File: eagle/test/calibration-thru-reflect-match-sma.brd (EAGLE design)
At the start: 10 x 44 mm, 6 parts, among them J1 142-0701-851, J2 142-0701-851, J3 142-0701-851, J4 142-0701-851

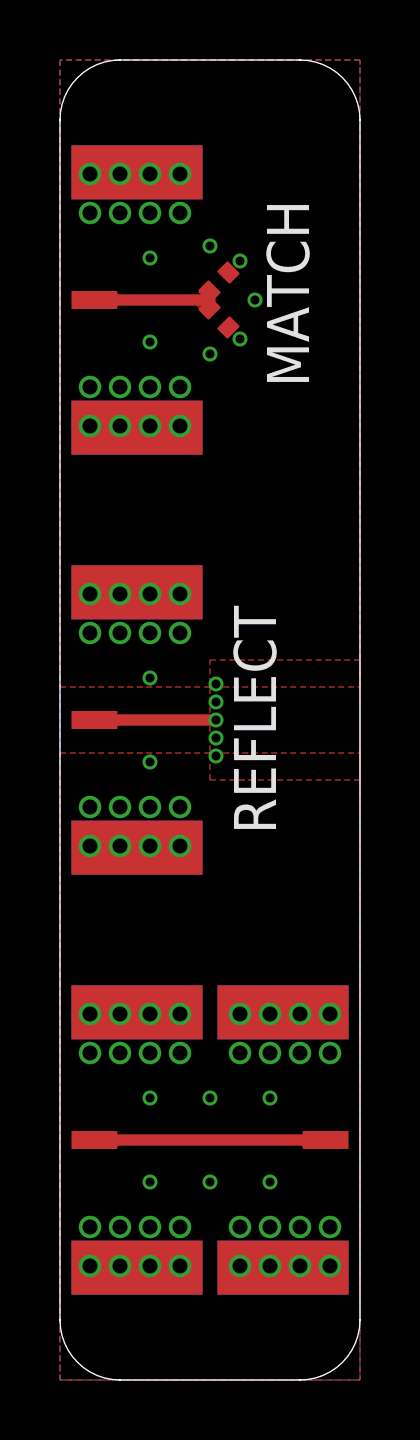
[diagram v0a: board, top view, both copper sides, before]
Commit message: Update TRM kit, add more stop mask around match
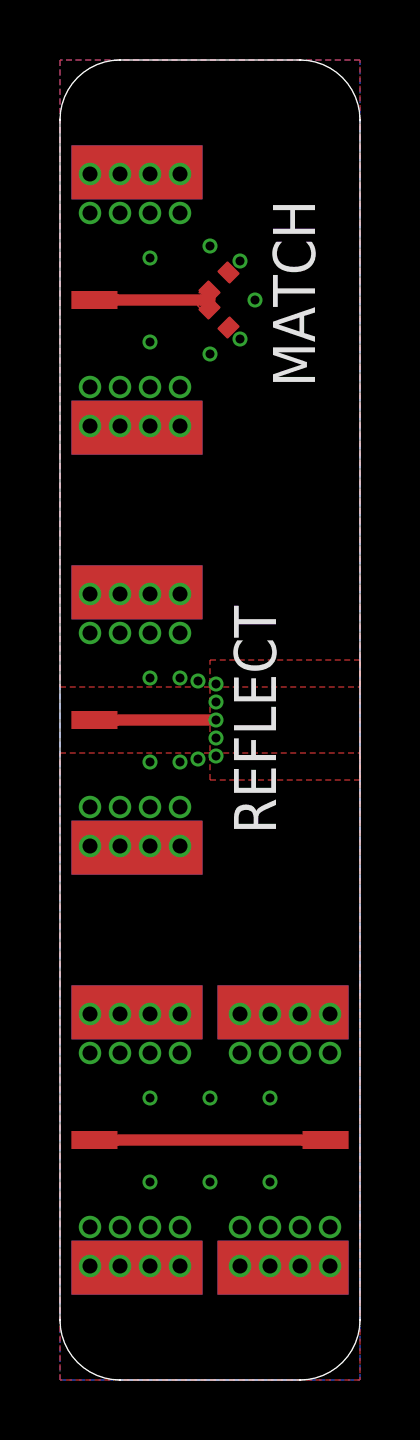
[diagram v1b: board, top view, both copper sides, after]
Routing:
- net GND: vias 84 -> 88
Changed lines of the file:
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@@
 <wire x1="2" y1="0" x2="8" y2="0" width="0" layer="20"/>
 <wire x1="8" y1="0" x2="10" y2="2" width="0" layer="20" curve="90"/>
-<text x="8.3" y="33.1" size="1.4" layer="21" font="vector" ratio="15" rot="R90">MATCH</text>
+<text x="8.5" y="33.1" size="1.4" layer="21" font="vector" ratio="15" rot="R90">MATCH</text>
 <text x="7.2" y="18.2" size="1.4" layer="21" font="vector" ratio="15" rot="R90">REFLECT</text>
 <wire x1="0" y1="36" x2="5" y2="36" width="2.1" layer="29"/>
 <wire x1="0" y1="22" x2="4" y2="22" width="2.1" layer="29"/>
 <wire x1="0" y1="8" x2="10" y2="8" width="2.1" layer="29"/>
+<circle x="4.9" y="36" radius="1.5" width="1.2" layer="29"/>
 </plain>
 <attributes>
@@
 <vertex x="5" y="24"/>
 </polygon>
+<via x="4" y="20.6" extent="1-16" drill="0.3"/>
+<via x="4.6" y="20.7" extent="1-16" drill="0.3"/>
+<via x="4.6" y="23.3" extent="1-16" drill="0.3"/>
+<via x="4" y="23.4" extent="1-16" drill="0.3"/>
 </signal>
 <signal name="MATCH" class="1">
